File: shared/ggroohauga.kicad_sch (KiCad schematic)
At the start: 11 parts

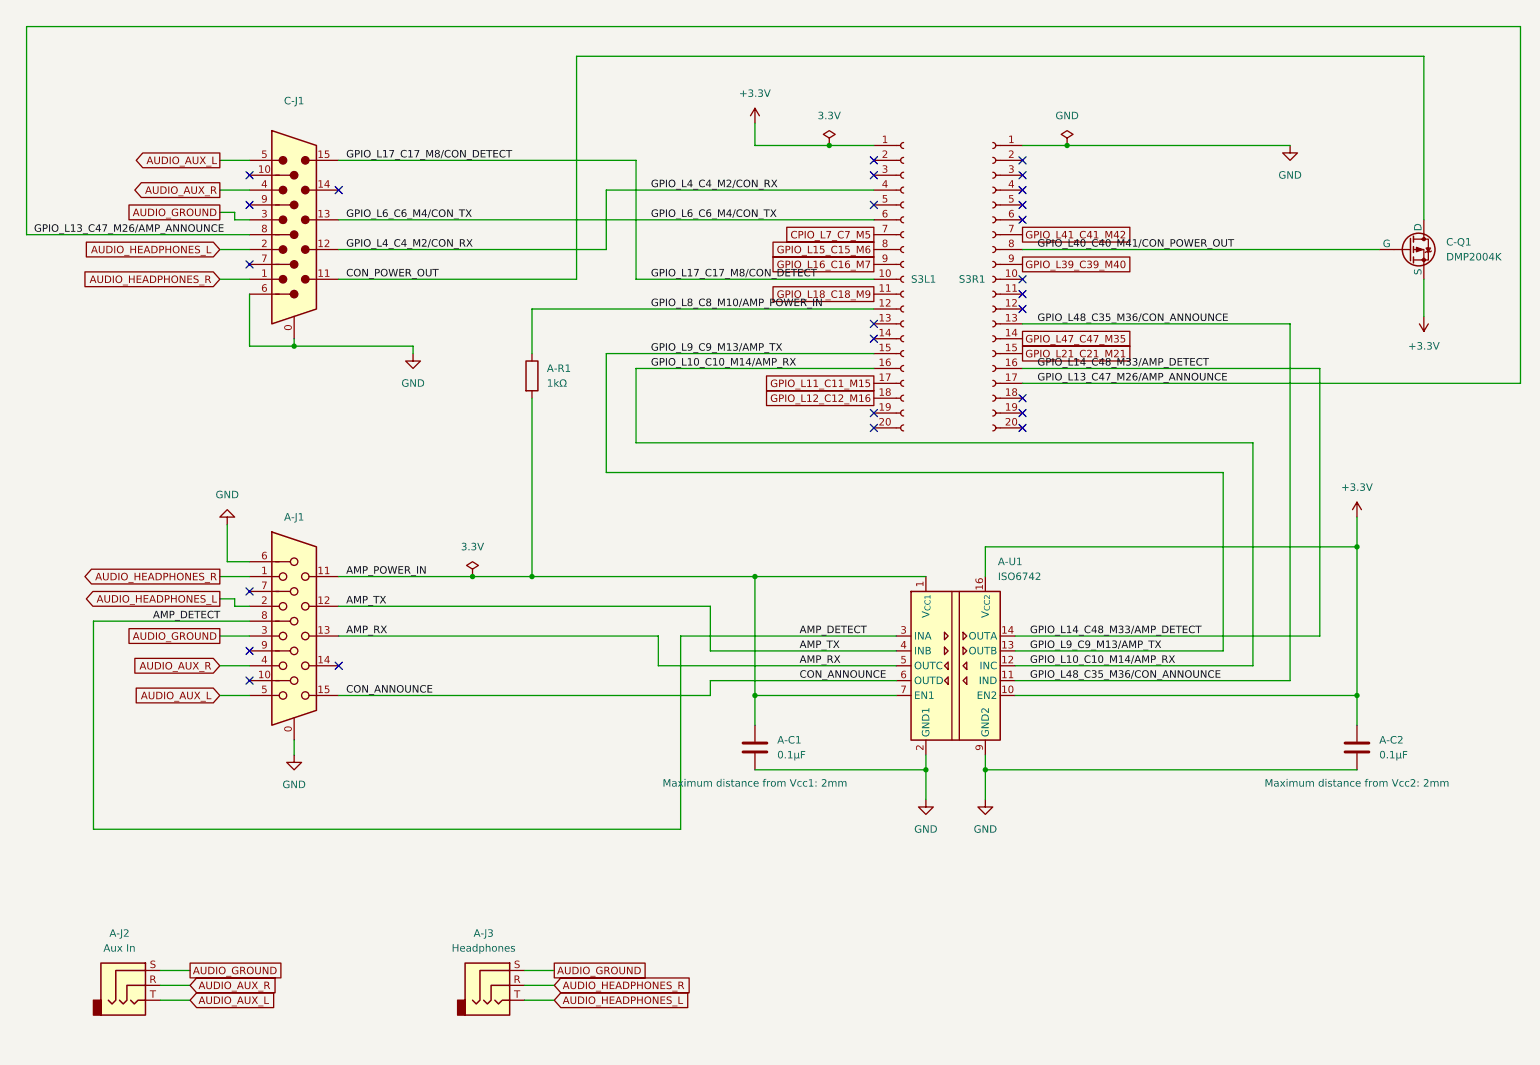
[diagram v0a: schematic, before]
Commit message: Reorganise schematic into multiple sheets and add 3 board identifier GPIOs
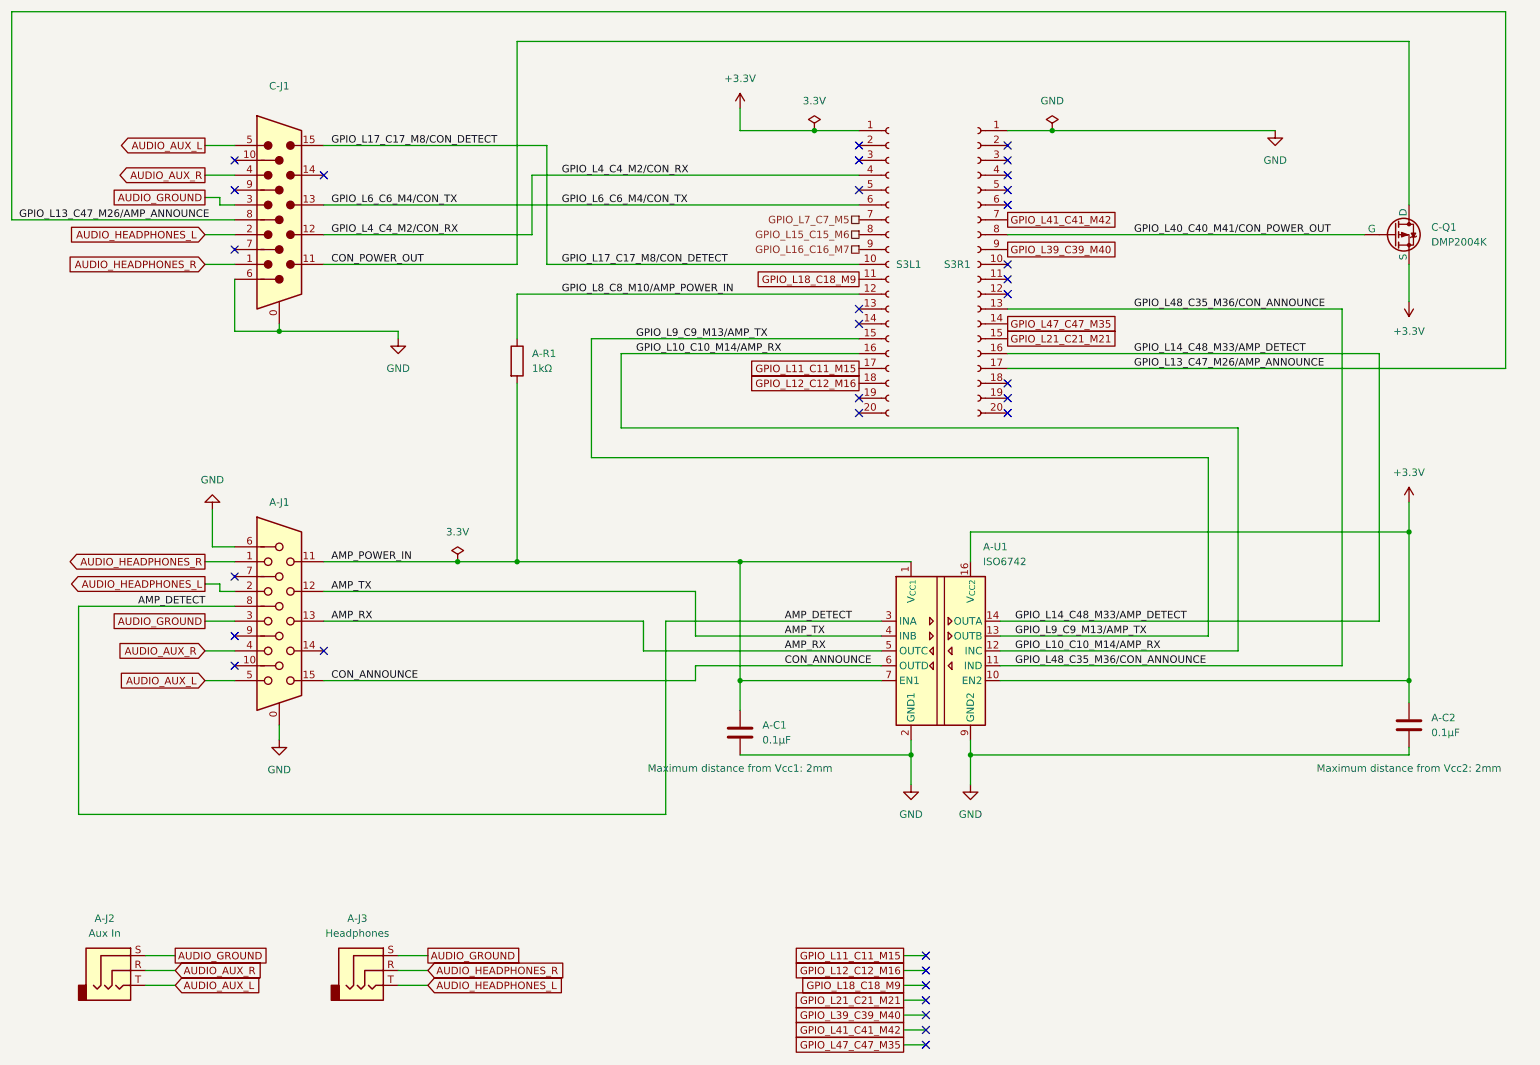
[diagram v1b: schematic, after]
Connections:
- net CPIO_L7_C7_M5 renamed GPIO_L7_C7_M5
- no-connect marks 26 -> 33
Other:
- moved on the sheet: A-C2, A-J1, A-J2, A-J3, A-U1, C-J1, C-Q1, S3L1, S3R1

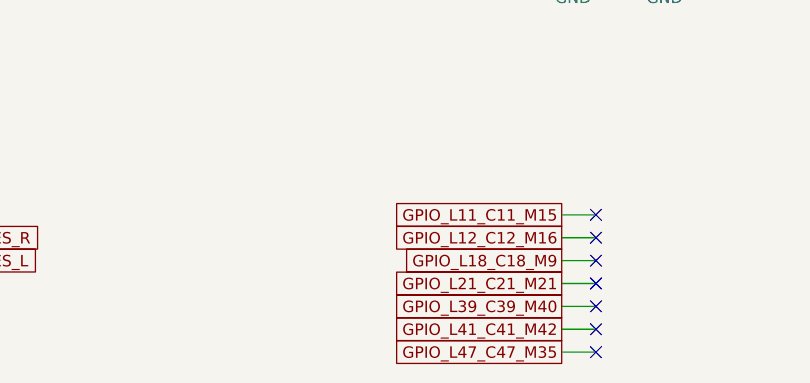
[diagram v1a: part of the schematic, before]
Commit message: Ground unused GPIOs
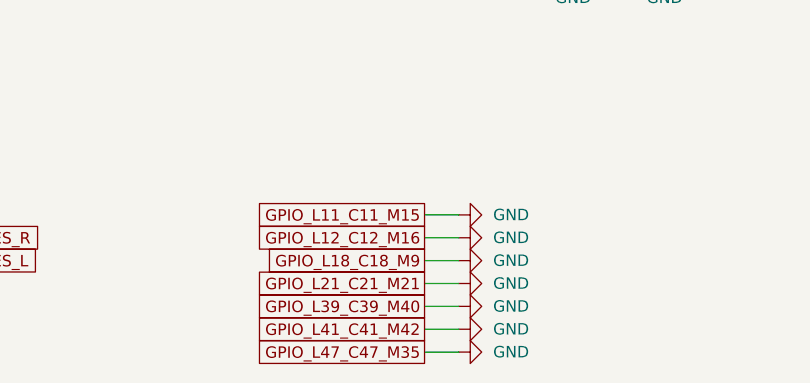
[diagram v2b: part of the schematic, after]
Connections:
- net GPIO_L11_C11_M15 is gone; now on net GND: S3L1.17 (Pin_17)
- net GPIO_L12_C12_M16 is gone; now on net GND: S3L1.18 (Pin_18)
- net GPIO_L18_C18_M9 is gone; now on net GND: S3L1.11 (Pin_11)
- net GPIO_L21_C21_M21 is gone; now on net GND: S3R1.15 (Pin_15)
- net GPIO_L39_C39_M40 is gone; now on net GND: S3R1.9 (Pin_9)
- net GPIO_L41_C41_M42 is gone; now on net GND: S3R1.7 (Pin_7)
- net GPIO_L47_C47_M35 is gone; now on net GND: S3R1.14 (Pin_14)
- no-connect marks 33 -> 26

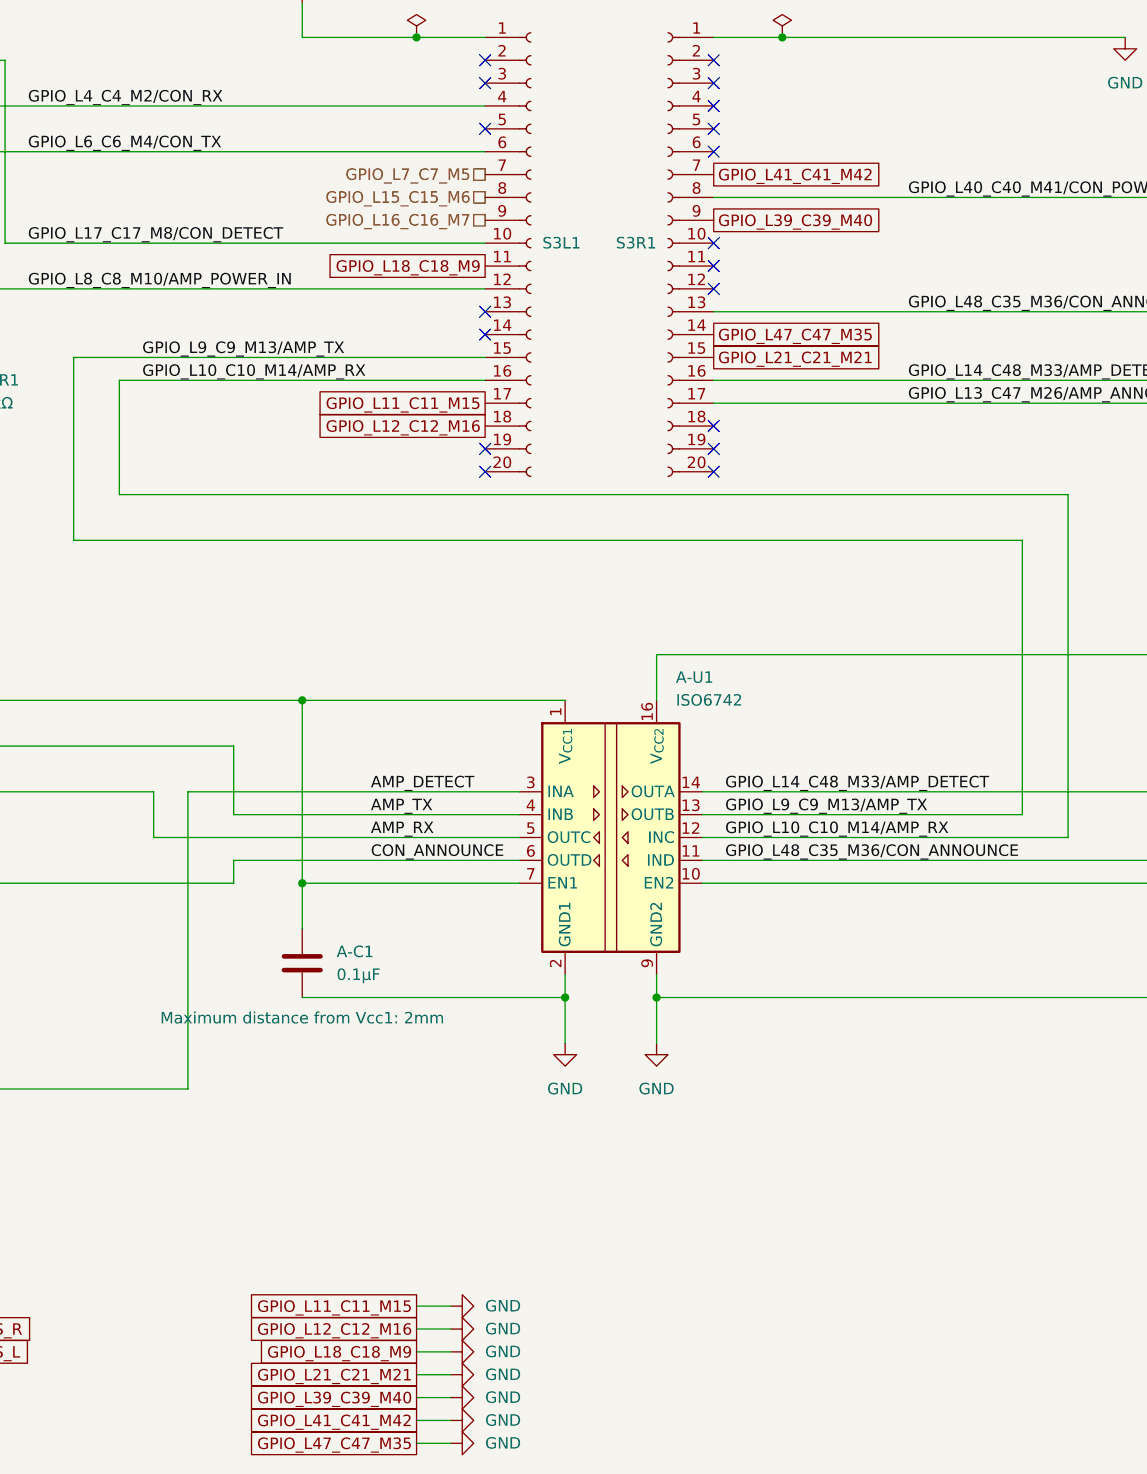
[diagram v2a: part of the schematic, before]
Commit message: Add "BOARD_ID" to the GPIOs for that and fix net names on unused GPIOs
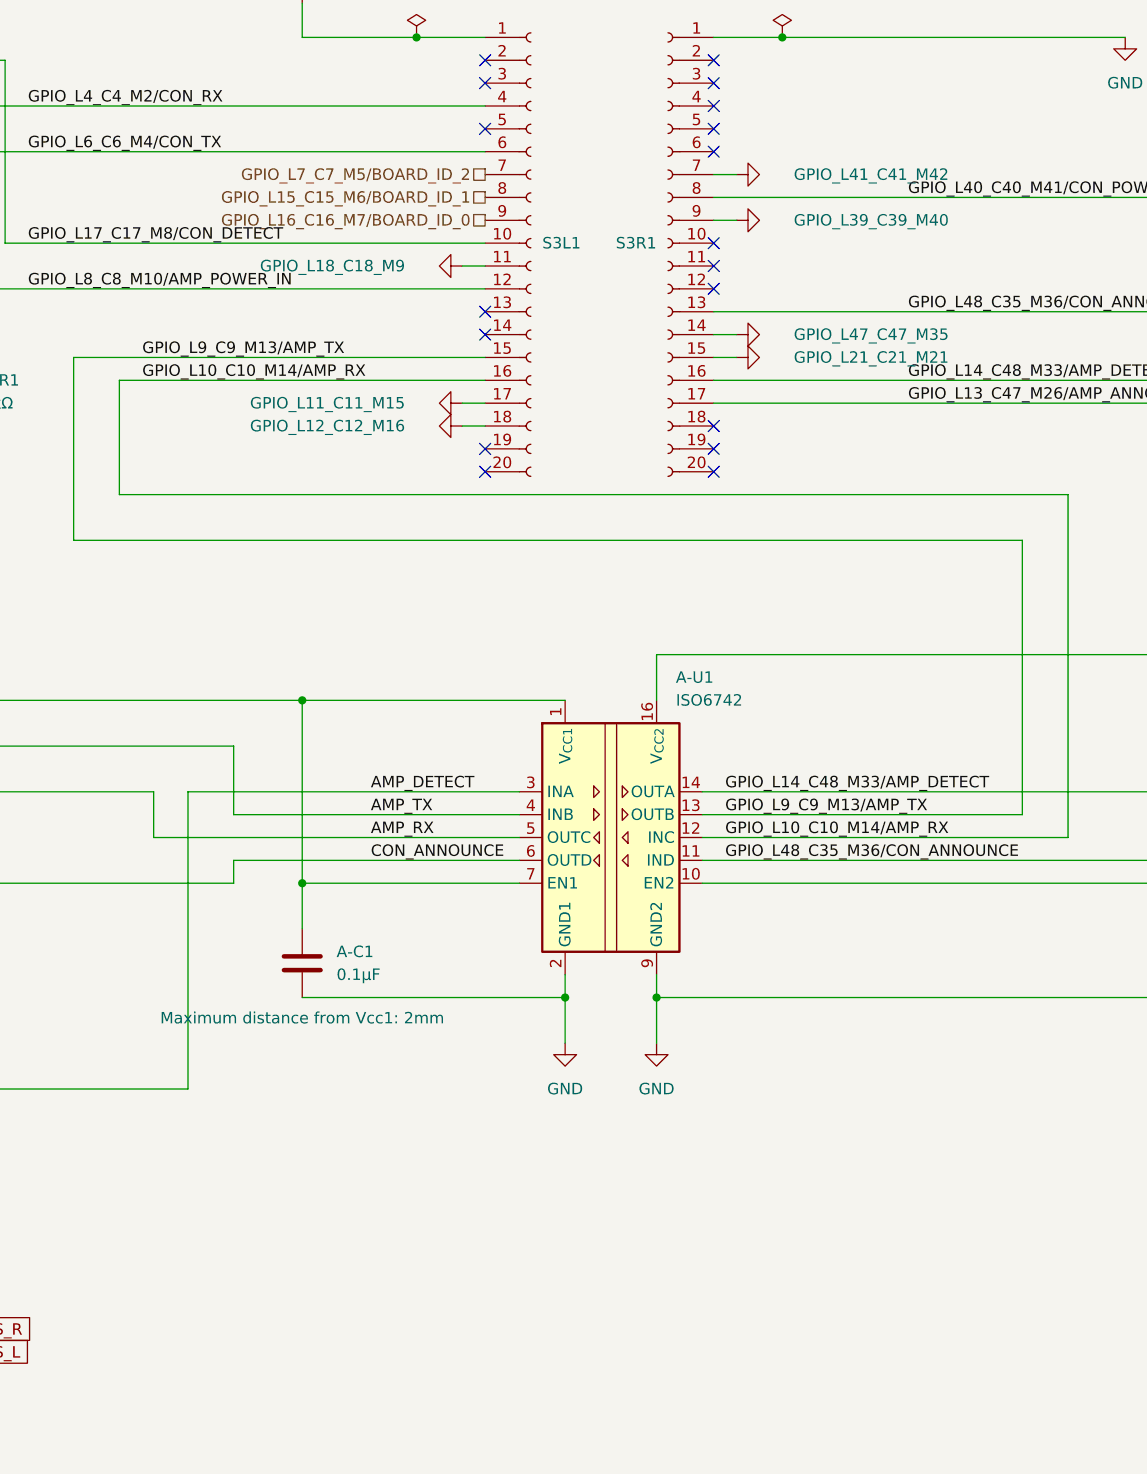
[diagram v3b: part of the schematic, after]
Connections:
- net GPIO_L15_C15_M6 renamed GPIO_L15_C15_M6/BOARD_ID_1
- net GPIO_L16_C16_M7 renamed GPIO_L16_C16_M7/BOARD_ID_0
- net GPIO_L7_C7_M5 renamed GPIO_L7_C7_M5/BOARD_ID_2
